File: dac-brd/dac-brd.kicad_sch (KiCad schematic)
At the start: 19 parts, among them J1 HTR, J2 I2C, J3 UART, U1 REF5030ID, U2 DAC5578xPW, U3 DAC5578xPW

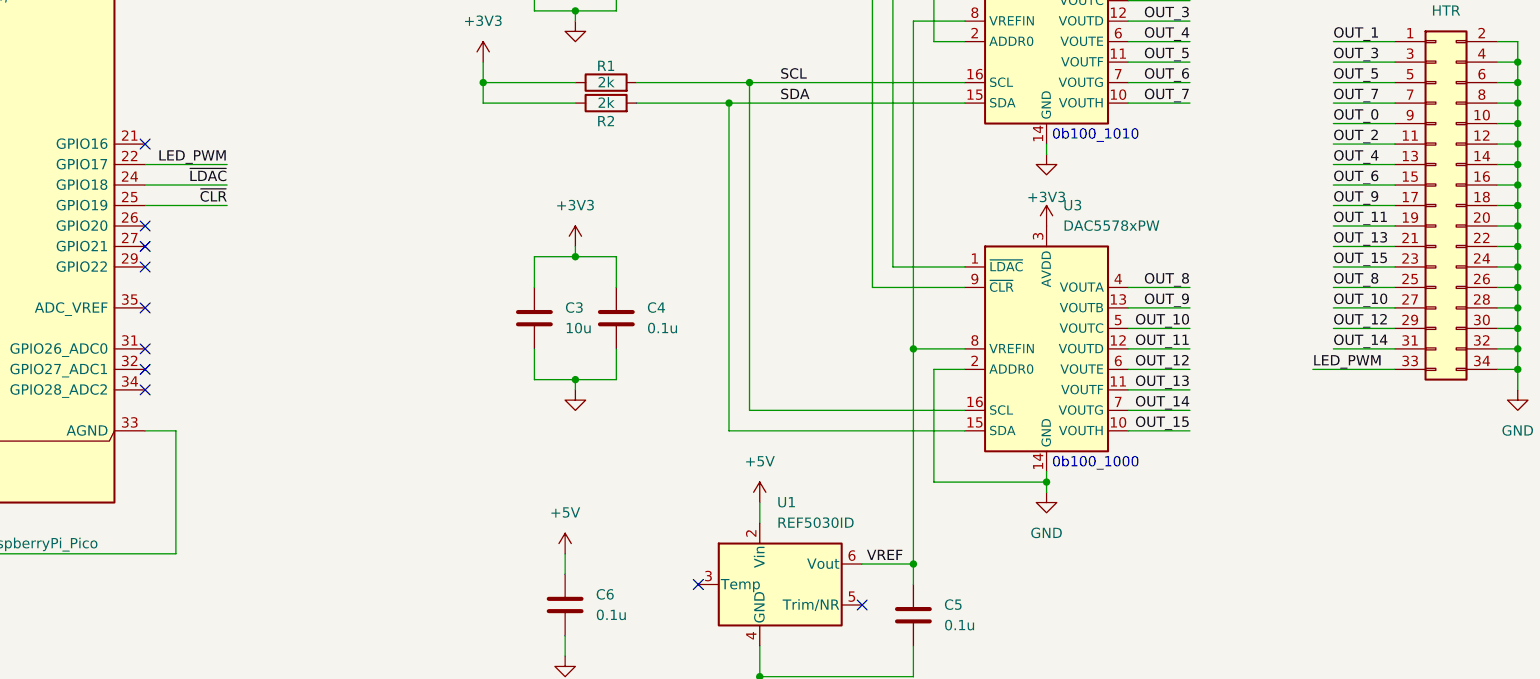
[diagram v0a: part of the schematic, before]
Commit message: Modified DAC, AMP v2 and Mezzanine to support AMP v3. Finished AMP v3 design.
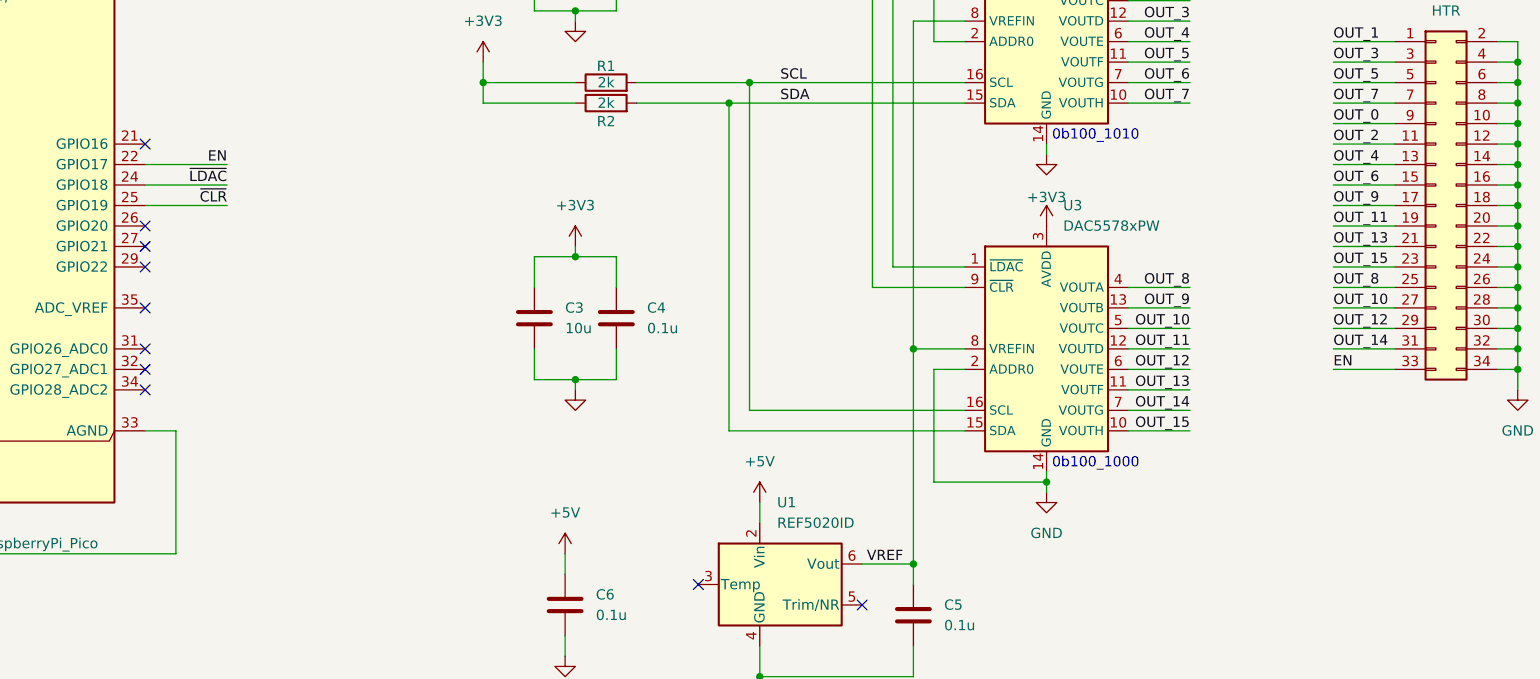
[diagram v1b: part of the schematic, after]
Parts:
- removed U1: REF5030ID, Package_SO:SOIC-8_3.9x4.9mm_P1.27mm, symbol Reference_Voltage:REF5030ID
- added U1: REF5020ID, Package_SO:SOIC-8_3.9x4.9mm_P1.27mm, symbol Reference_Voltage:REF5020ID
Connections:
- net +5V: now also U1.2 (Vin)
- net GND: now also U1.4 (GND)
- net VREF: now also U1.6 (Vout)
- net LED_PWM renamed EN
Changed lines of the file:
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@@
 	(wire
 		(pts
-			(xy 238.76 110.49) (xy 248.92 110.49)
+			(xy 241.3 110.49) (xy 248.92 110.49)
 		)
 		(stroke
@@
 		)
 	)
-	(label "LED_PWM"
-		(at 238.76 110.49 0)
+	(label "EN"
+		(at 241.3 110.49 0)
 		(effects
 			(font
@@
 		)
 	)
-	(label "LED_PWM"
+	(label "EN"
 		(at 104.14 85.09 180)
 		(effects
@@
 	)
 	(symbol
-		(lib_id "Reference_Voltage:REF5030ID")
-		(at 172.72 137.16 0)
-		(unit 1)
-		(exclude_from_sim no)
-		(in_bom yes)
-		(on_board yes)
-		(dnp no)
-		(fields_autoplaced yes)
-		(property "Reference" "U1"
-			(at 172.3233 127 0)
-			(effects
-				(font
-					(size 1.27 1.27)
-				)
-				(justify left)
-			)
-		)
-		(property "Value" "REF5030ID"
-			(at 172.3233 129.54 0)
-			(effects
-				(font
-					(size 1.27 1.27)
-				)
-				(justify left)
-			)
-		)
-		(property "Footprint" "Package_SO:SOIC-8_3.9x4.9mm_P1.27mm"
-			(at 170.815 143.51 0)
-			(effects
-				(font
-					(size 1.27 1.27)
-					(italic yes)
-				)
-				(justify left)
-				(hide yes)
-			)
-		)
-		(property "Datasheet" "https://www.ti.com/lit/ds/symlink/ref50.pdf"
-			(at 171.45 137.16 0)
-			(effects
-				(font
-					(size 1.27 1.27)
-					(italic yes)
-				)
-				(hide yes)
-			)
-		)
-		(property "Description" "3V 0.05% 10mA Low Noise Precision Voltage Reference, SO-8"
-			(at 172.72 137.16 0)
-			(effects
-				(font
-					(size 1.27 1.27)
-				)
-				(hide yes)
-			)
-		)
-		(pin "5"
-		)
-		(pin "1"
-		)
-		(pin "7"
-		)
-		(pin "2"
-		)
-		(pin "4"
-		)
-		(pin "8"
-		)
-		(pin "6"
-		)
-		(pin "3"
-		)
-		(instances
-			(project ""
-				(path "/42f52ef8-91b5-4b39-8096-c8af77b54354"
-					(reference "U1")
-					(unit 1)
-				)
-			)
-		)
-	)
-	(symbol
 		(lib_id "Device:C")
 		(at 152.4 104.14 0)
@@
 					(unit 1)
 				)
+			)
+		)
+	)
+	(symbol
+		(lib_id "Reference_Voltage:REF5020ID")
+		(at 172.72 137.16 0)
+		(unit 1)
+		(exclude_from_sim no)
+		(in_bom yes)
+		(on_board yes)
+		(dnp no)
+		(fields_autoplaced yes)
+		(property "Reference" "U1"
+			(at 172.3233 127 0)
+			(effects
+				(font
+					(size 1.27 1.27)
+				)
+				(justify left)
+			)
+		)
+		(property "Value" "REF5020ID"
+			(at 172.3233 129.54 0)
+			(effects
+				(font
+					(size 1.27 1.27)
+				)
+				(justify left)
+			)
+		)
+		(property "Footprint" "Package_SO:SOIC-8_3.9x4.9mm_P1.27mm"
+			(at 170.815 143.51 0)
+			(effects
+				(font
+					(size 1.27 1.27)
+					(italic yes)
+				)
+				(justify left)
+				(hide yes)
+			)
+		)
+		(property "Datasheet" "https://www.ti.com/lit/ds/symlink/ref50.pdf"
+			(at 171.45 137.16 0)
+			(effects
+				(font
+					(size 1.27 1.27)
+					(italic yes)
+				)
+				(hide yes)
+			)
+		)
+		(property "Description" "2.048V 0.05% 10mA Low Noise Precision Voltage Reference, SO-8"
+			(at 172.72 137.16 0)
+			(effects
+				(font
+					(size 1.27 1.27)
+				)
+				(hide yes)
+			)
+		)
+		(pin "3"
+		)
+		(pin "1"
+		)
+		(pin "7"
+		)
+		(pin "2"
+		)
+		(pin "4"
+		)
+		(pin "8"
+		)
+		(pin "6"
+		)
+		(pin "5"
+		)
+		(instances
+			(project ""
+				(path "/42f52ef8-91b5-4b39-8096-c8af77b54354"
+					(reference "U1")
+					(unit 1)
+				)

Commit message: Final review with Joe
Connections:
- net +3V3: now also C6.1, U1.2 (Vin)
- net +5V: no longer C6.1, U1.2 (Vin)
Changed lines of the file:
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@@
+	(symbol
+		(lib_id "power:+3V3")
+		(at 146.05 133.35 0)
+		(unit 1)
+		(exclude_from_sim no)
+		(in_bom yes)
+		(on_board yes)
+		(dnp no)
+		(fields_autoplaced yes)
+		(property "Reference" "#PWR014"
+			(at 146.05 137.16 0)
+			(effects
+				(font
+					(size 1.27 1.27)
+				)
+				(hide yes)
+			)
+		)
+		(property "Value" "+3V3"
+			(at 146.05 128.27 0)
+			(effects
+				(font
+					(size 1.27 1.27)
+				)
+			)
+		)
+		(property "Footprint" ""
+			(at 146.05 133.35 0)
+			(effects
+				(font
+					(size 1.27 1.27)
+				)
+				(hide yes)
+			)
+		)
+		(property "Datasheet" ""
+			(at 146.05 133.35 0)
+			(effects
+				(font
+					(size 1.27 1.27)
+				)
+				(hide yes)
+			)
+		)
+		(property "Description" "Power symbol creates a global label with name \"+3V3\""
+			(at 146.05 133.35 0)
+			(effects
+				(font
+					(size 1.27 1.27)
+				)
+				(hide yes)
+			)
+		)
+		(pin "1"
+		)
+		(instances
+			(project "dac-brd"
+				(path "/42f52ef8-91b5-4b39-8096-c8af77b54354"
+					(reference "#PWR014")
+					(unit 1)
+				)
+			)
+		)
+	)
 	(symbol
 		(lib_id "power:+3V3")
@@
 	)
 	(symbol
+		(lib_id "power:+3V3")
+		(at 170.18 127 0)
+		(unit 1)
+		(exclude_from_sim no)
+		(in_bom yes)
+		(on_board yes)
+		(dnp no)
+		(fields_autoplaced yes)
+		(property "Reference" "#PWR011"
+			(at 170.18 130.81 0)
+			(effects
+				(font
+					(size 1.27 1.27)
+				)
+				(hide yes)
+			)
+		)
+		(property "Value" "+3V3"
+			(at 170.18 121.92 0)
+			(effects
+				(font
+					(size 1.27 1.27)
+				)
+			)
+		)
+		(property "Footprint" ""
+			(at 170.18 127 0)
+			(effects
+				(font
+					(size 1.27 1.27)
+				)
+				(hide yes)
+			)
+		)
+		(property "Datasheet" ""
+			(at 170.18 127 0)
+			(effects
+				(font
+					(size 1.27 1.27)
+				)
+				(hide yes)
+			)
+		)
+		(property "Description" "Power symbol creates a global label with name \"+3V3\""
+			(at 170.18 127 0)
+			(effects
+				(font
+					(size 1.27 1.27)
+				)
+				(hide yes)
+			)
+		)
+		(pin "1"
+		)
+		(instances
+			(project "dac-brd"
+				(path "/42f52ef8-91b5-4b39-8096-c8af77b54354"
+					(reference "#PWR011")
+					(unit 1)
+				)
+			)
+		)
+	)
+	(symbol
 		(lib_id "Mechanical:MountingHole_Pad")
 		(at 63.5 160.02 0)
@@
 	)
 	(symbol
-		(lib_id "power:+5V")
-		(at 146.05 133.35 0)
-		(unit 1)
-		(exclude_from_sim no)
-		(in_bom yes)
-		(on_board yes)
-		(dnp no)
-		(fields_autoplaced yes)
-		(property "Reference" "#PWR014"
-			(at 146.05 137.16 0)
-			(effects
-				(font
-					(size 1.27 1.27)
-				)
-				(hide yes)
-			)
-		)
-		(property "Value" "+5V"
-			(at 146.05 128.27 0)
-			(effects
-				(font
-					(size 1.27 1.27)
-				)
-			)
-		)
-		(property "Footprint" ""
-			(at 146.05 133.35 0)
-			(effects
-				(font
-					(size 1.27 1.27)
-				)
-				(hide yes)
-			)
-		)
-		(property "Datasheet" ""
-			(at 146.05 133.35 0)
-			(effects
-				(font
-					(size 1.27 1.27)
-				)
-				(hide yes)
-			)
-		)
-		(property "Description" "Power symbol creates a global label with name \"+5V\""
-			(at 146.05 133.35 0)
-			(effects
-				(font
-					(size 1.27 1.27)
-				)
-				(hide yes)
-			)
-		)
-		(pin "1"
-		)
-		(instances
-			(project "dac-brd"
-				(path "/42f52ef8-91b5-4b39-8096-c8af77b54354"
-					(reference "#PWR014")
-					(unit 1)
-				)
-			)
-		)
-	)
-	(symbol
 		(lib_id "Device:C")
 		(at 142.24 58.42 0)
@@
 					(unit 1)
 				)
-			)
-		)
-	)
-	(symbol
-		(lib_id "power:+5V")
-		(at 170.18 127 0)
-		(unit 1)
-		(exclude_from_sim no)
-		(in_bom yes)
-		(on_board yes)
-		(dnp no)
-		(fields_autoplaced yes)
-		(property "Reference" "#PWR011"
-			(at 170.18 130.81 0)
-			(effects
-				(font
-					(size 1.27 1.27)
-				)
-				(hide yes)
-			)
-		)
-		(property "Value" "+5V"
-			(at 170.18 121.92 0)
-			(effects
-				(font
-					(size 1.27 1.27)
-				)
-			)
-		)
-		(property "Footprint" ""
-			(at 170.18 127 0)
-			(effects
-				(font
-					(size 1.27 1.27)
-				)
-				(hide yes)
-			)
-		)
-		(property "Datasheet" ""
-			(at 170.18 127 0)
-			(effects
-				(font
-					(size 1.27 1.27)
-				)
-				(hide yes)
-			)
-		)
-		(property "Description" "Power symbol creates a global label with name \"+5V\""
-			(at 170.18 127 0)
-			(effects
-				(font
-					(size 1.27 1.27)
-				)
-				(hide yes)
-			)
-		)
-		(pin "1"
-		)
-		(instances
-			(project "dac-brd"
-				(path "/42f52ef8-91b5-4b39-8096-c8af77b54354"
-					(reference "#PWR011")
-					(unit 1)
-				)

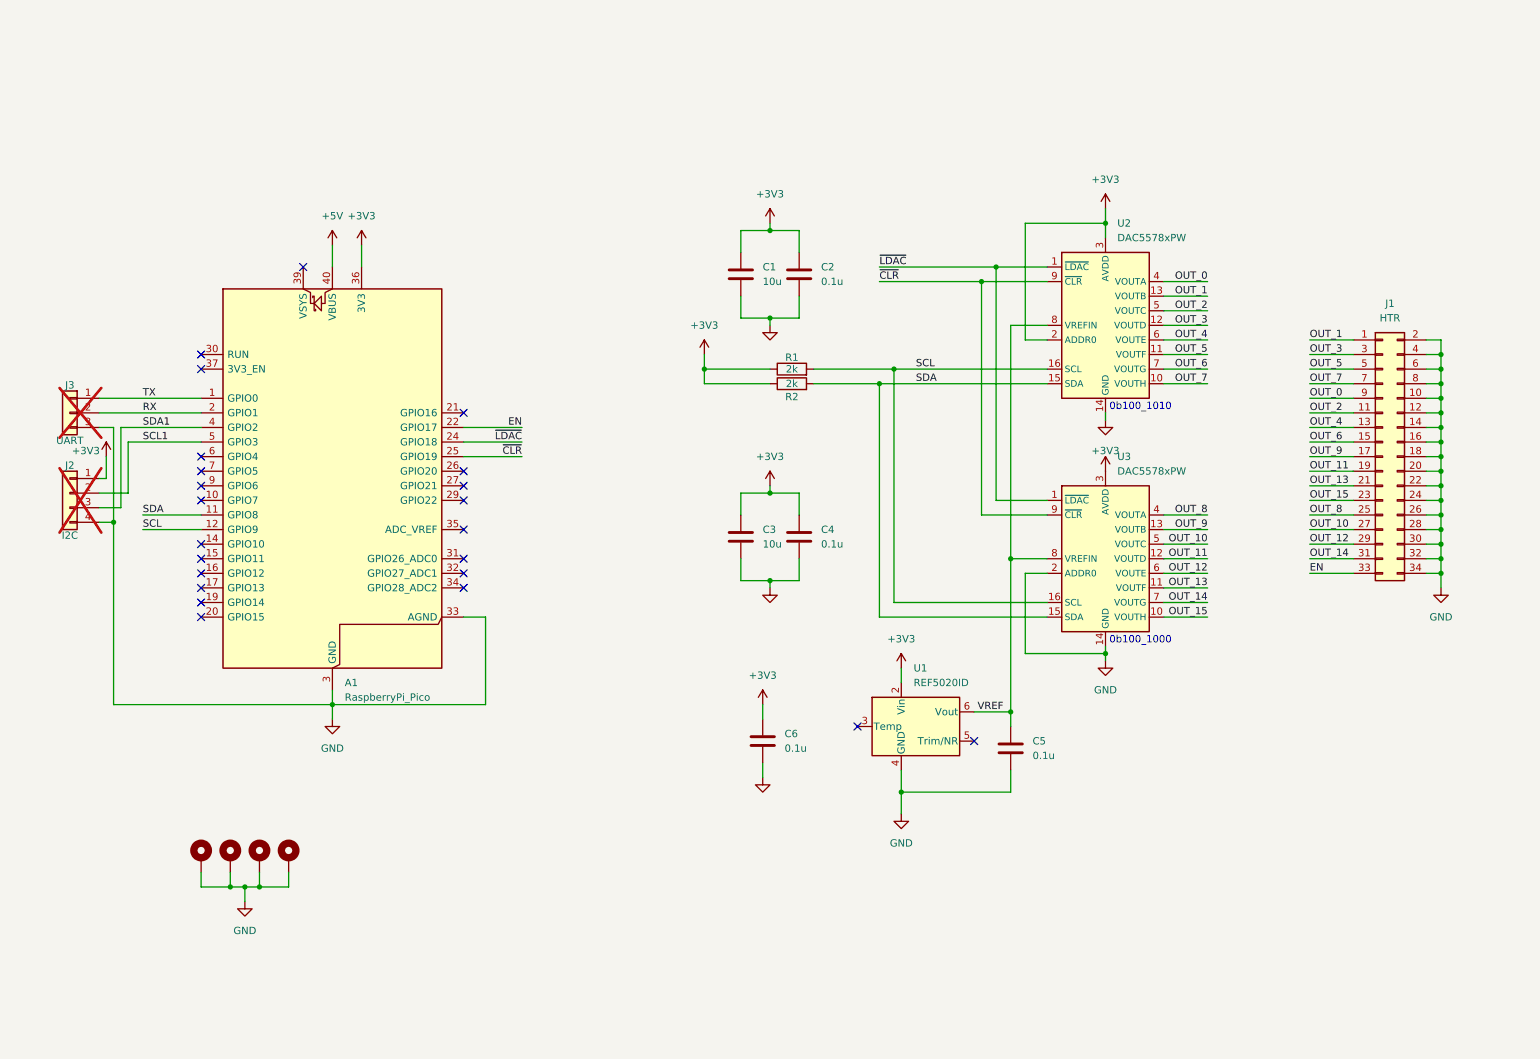
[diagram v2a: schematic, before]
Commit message: Tested DAC and INA, doing new boards
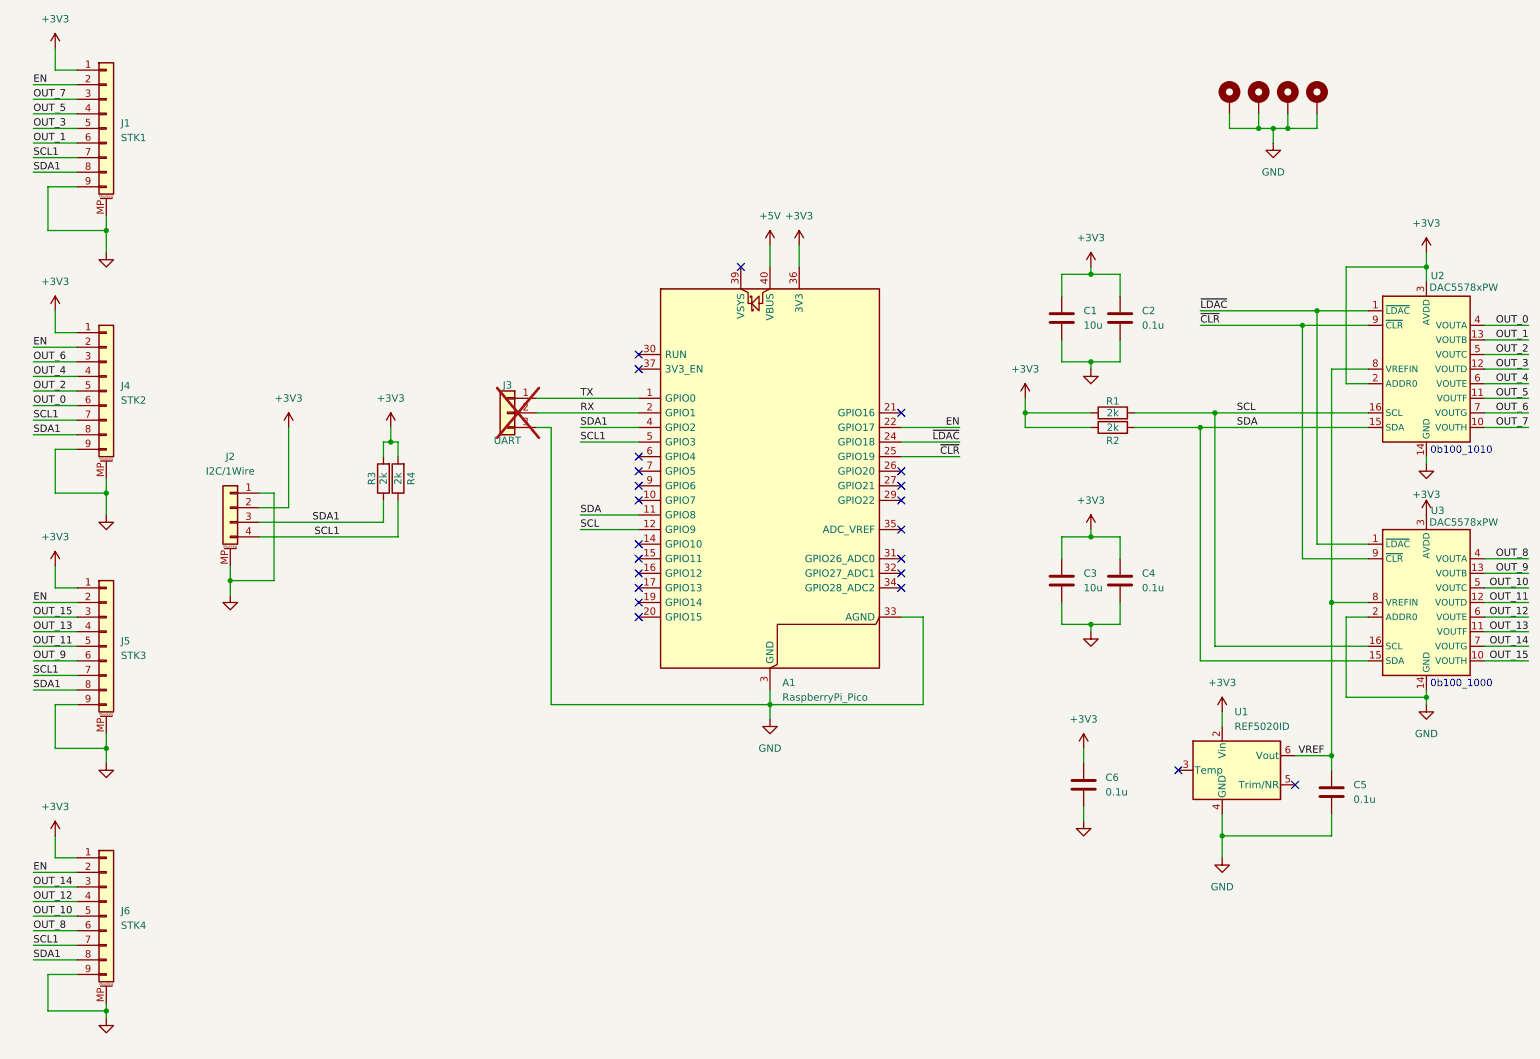
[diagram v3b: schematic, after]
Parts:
- removed J1: HTR, Connector_PinHeader_2.54mm:PinHeader_2x17_P2.54mm_Vertical, symbol Connector_Generic:Conn_02x17_Odd_Even
- removed J2: I2C, Connector_PinHeader_2.54mm:PinHeader_1x04_P2.54mm_Vertical, symbol Connector_Generic:Conn_01x04
- added J1: STK1, Connector_Molex:Molex_PicoBlade_53261-0971_1x09-1MP_P1.25mm_Horizontal, symbol Connector_Generic_MountingPin:Conn_01x09_MountingPin
- added J2: I2C/1Wire, Connector_JST:JST_SH_BM04B-SRSS-TB_1x04-1MP_P1.00mm_Vertical, symbol Connector_Generic_MountingPin:Conn_01x04_MountingPin
- added J4: STK2, Connector_Molex:Molex_PicoBlade_53261-0971_1x09-1MP_P1.25mm_Horizontal, symbol Connector_Generic_MountingPin:Conn_01x09_MountingPin
- added J5: STK3, Connector_Molex:Molex_PicoBlade_53261-0971_1x09-1MP_P1.25mm_Horizontal, symbol Connector_Generic_MountingPin:Conn_01x09_MountingPin
- added J6: STK4, Connector_Molex:Molex_PicoBlade_53261-0971_1x09-1MP_P1.25mm_Horizontal, symbol Connector_Generic_MountingPin:Conn_01x09_MountingPin
- added R3, R4: 2k, Resistor_SMD:R_0805_2012Metric, symbol Device:R
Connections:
- net +3V3: now also J1.1 (Pin_1), J2.2 (Pin_2), J4.1 (Pin_1), J5.1 (Pin_1), J6.1 (Pin_1), R3.2, R4.2
- net EN: now also J1.2 (Pin_2), J4.2 (Pin_2), J5.2 (Pin_2), J6.2 (Pin_2)
- net GND: now also J1.9 (Pin_9), J1.MP (MountPin), J2.1 (Pin_1), J2.MP (MountPin), J4.9 (Pin_9), J4.MP (MountPin), J5.9 (Pin_9), J5.MP (MountPin), J6.9 (Pin_9), J6.MP (MountPin)
- net OUT_0: now also J4.6 (Pin_6)
- net OUT_1: now also J1.6 (Pin_6)
- net OUT_10: now also J6.5 (Pin_5)
- net OUT_11: now also J5.5 (Pin_5)
- net OUT_12: now also J6.4 (Pin_4)
- net OUT_13: now also J5.4 (Pin_4)
- net OUT_14: now also J6.3 (Pin_3)
- net OUT_15: now also J5.3 (Pin_3)
- net OUT_2: now also J4.5 (Pin_5)
- net OUT_3: now also J1.5 (Pin_5)
- net OUT_4: now also J4.4 (Pin_4)
- net OUT_5: now also J1.4 (Pin_4)
- net OUT_6: now also J4.3 (Pin_3)
- net OUT_7: now also J1.3 (Pin_3)
- net OUT_8: now also J6.6 (Pin_6)
- net OUT_9: now also J5.6 (Pin_6)
- net SCL1: now also J1.7 (Pin_7), J2.4 (Pin_4), J4.7 (Pin_7), J5.7 (Pin_7), J6.7 (Pin_7), R4.1
- net SDA1: now also J1.8 (Pin_8), J2.3 (Pin_3), J4.8 (Pin_8), J5.8 (Pin_8), J6.8 (Pin_8), R3.1
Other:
- moved on the sheet: A1, C1, C2, C3, C4, C5, C6, J3, R1, R2, U1, U2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
